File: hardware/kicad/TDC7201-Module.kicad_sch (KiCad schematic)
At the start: 5 parts, among them U2 AMS1117-3.3, U3 TDC7201, U4 TLV3501, U5 TLV3501, U7 ESP32-C3-WROOM-02U-N4

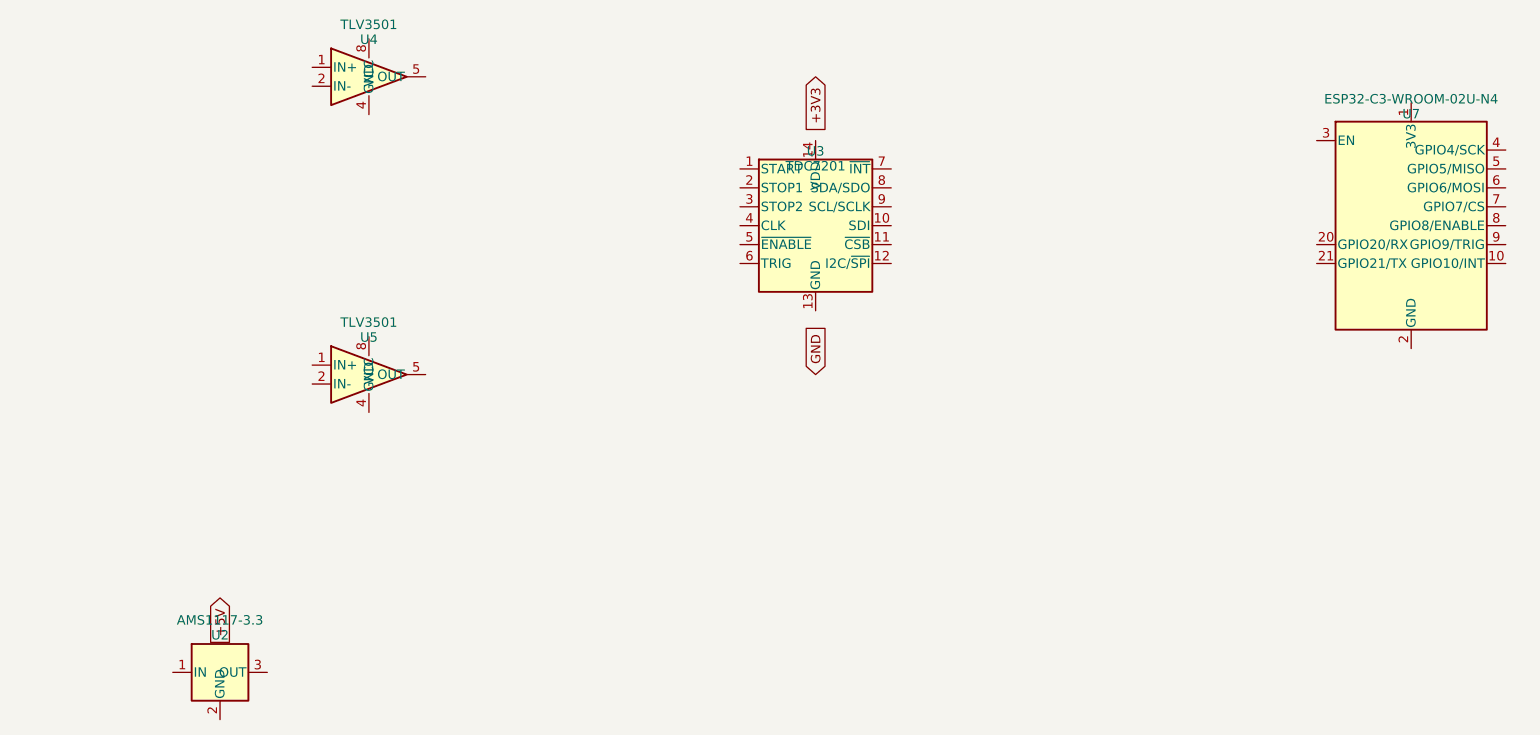
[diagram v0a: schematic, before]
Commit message: Regenerate valid KiCad 7.0 PCB and schematic files
- TDC7201-Module.kicad_pcb: complete rewrite with valid KiCad 7.0
  S-expression syntax (version 20221018). Removes all ;; comments,
  invalid (module ...) / (capacitor ...) / (inductor ...) syntax.
  Adds proper (net 0..15) declarations with numeric IDs, valid
  (footprint ...) blocks for all ICs/connectors with numeric net
  references in pads and vias, 4-layer stackup (F.Cu/In1.Cu/In2.Cu/B.Cu),
  80x50mm board outline on Edge.Cuts, and GND via stitching.
- TDC7201-Module.kicad_sch: complete rewrite removing all ;; comments
  and fixing (net_label ...) to valid (label ...) syntax. Adds
  complete lib_symbols section, properly closed symbol instances,
  global_label declarations, and wire connections.

Agent-Logs-Url: https://github.com/jeffkarney/TDC7201-GPSDO-Module/sessions/249e8e96-76a3-4c3b-a7cb-0897e226d90f

Co-authored-by: jeffkarney <201882+jeffkarney@users.noreply.github.com>
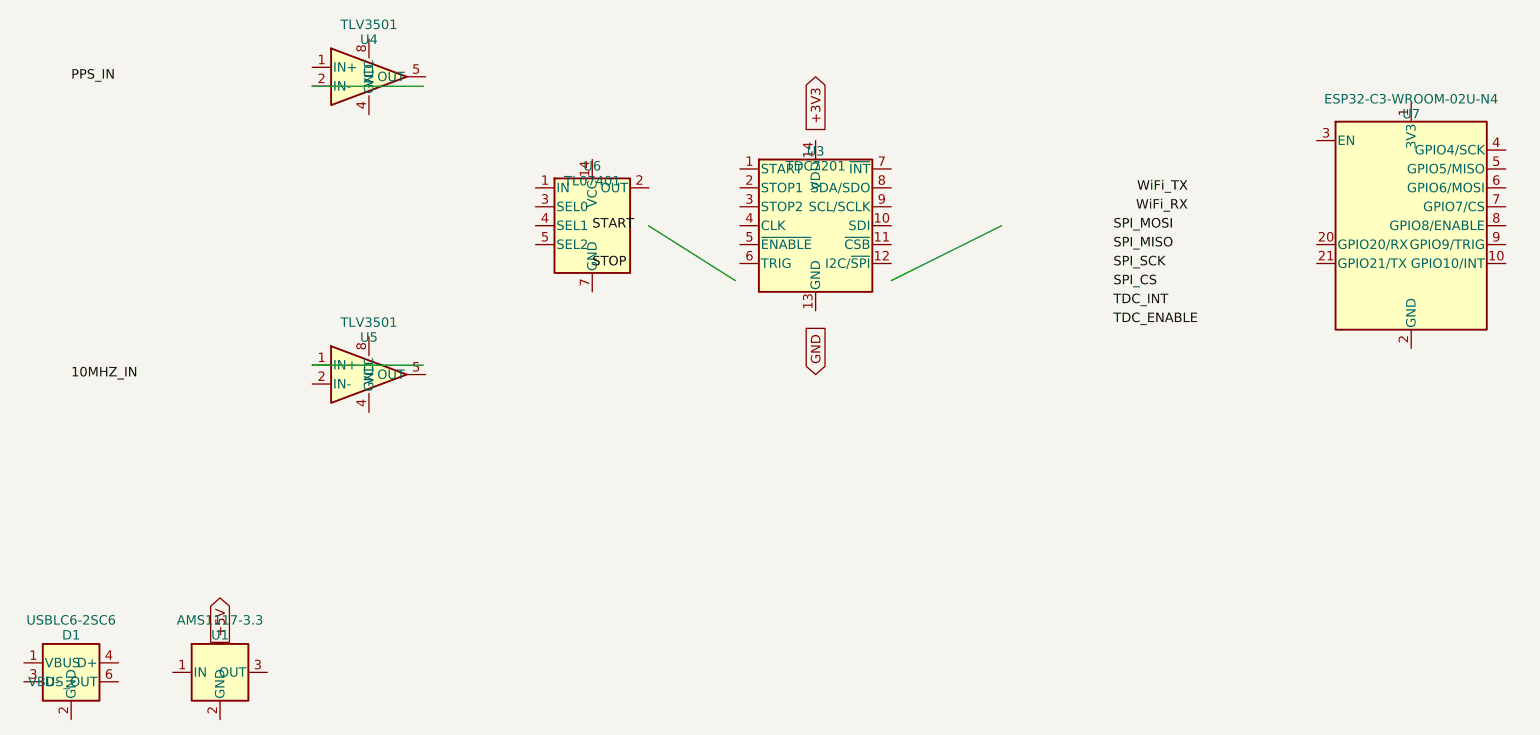
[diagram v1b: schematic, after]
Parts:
- removed U2: AMS1117-3.3, symbol AMS1117-3.3
- added D1: USBLC6-2SC6, Package_TO_SOT_SMD:SOT-23-6, symbol USBLC6-2SC6
- added U1: AMS1117-3.3, Package_TO_SOT_SMD:SOT-223-3_TabPin2, symbol AMS1117-3.3
- added U6: TL07401, Package_SO:TSSOP-14_4.4x5mm_P0.65mm, symbol TL07401
- U4, U5: footprint (none) -> Package_SO:TSSOP-8_3x3mm_P0.65mm
- U7: footprint (none) -> RF_Module:ESP32-C3-WROOM-02
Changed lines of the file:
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@@
 (kicad_sch
-  (version 20231120)
+  (version 20221018)
   (generator "eeschema")
-  (generator_version "7.0")
   (paper "A3")
   (title_block
@@
     (rev "1.0")
     (company "jeffkarney")
-    (comment 1 "4-Layer PCB – JLCPCB JLC04161H-7628")
+    (comment 1 "4-Layer PCB - JLCPCB JLC04161H-7628")
     (comment 2 "ESP32-C3-WROOM-02U-N4 + dual TLV3501 + TDC7201")
     (comment 3 "USB-C 5V input, 3.3V LDO, SPI interface")
   )
-  ;; -------------------------------------------------------------------------
-  ;; Schematic instances (placement)
-  ;; -------------------------------------------------------------------------
-  ;; U3 – TDC7201
   (symbol (lib_id "TDC7201") (at 120 80 0) (unit 1)
     (in_bom yes) (on_board yes)
     (uuid "tdc7201-main-u3")
-    (property "Reference" "U3" (at 120 70 0))
-    (property "Value" "TDC7201" (at 120 72 0))
-    (property "Footprint" "Package_SO:TSSOP-16_4.4x5mm_P0.65mm" (at 0 0 0) (effects (hide yes)))
+    (property "Reference" "U3" (at 120 70 0)
+      (effects (font (size 1.27 1.27))))
+    (property "Value" "TDC7201" (at 120 72 0)
+      (effects (font (size 1.27 1.27))))
+    (property "Footprint" "Package_SO:TSSOP-16_4.4x5mm_P0.65mm" (at 0 0 0)
+      (effects (font (size 1.27 1.27)) (hide yes)))
+    (property "Datasheet" "" (at 0 0 0)
+      (effects (font (size 1.27 1.27)) (hide yes)))
   )
-  ;; U4 – TLV3501 (PPS channel)
   (symbol (lib_id "TLV3501") (at 60 60 0) (unit 1)
     (in_bom yes) (on_board yes)
     (uuid "tlv3501-pps-u4")
-    (property "Reference" "U4" (at 60 55 0))
-    (property "Value" "TLV3501" (at 60 53 0))
+    (property "Reference" "U4" (at 60 55 0)
+      (effects (font (size 1.27 1.27))))
+    (property "Value" "TLV3501" (at 60 53 0)
+      (effects (font (size 1.27 1.27))))
+    (property "Footprint" "Package_SO:TSSOP-8_3x3mm_P0.65mm" (at 0 0 0)
+      (effects (font (size 1.27 1.27)) (hide yes)))
+    (property "Datasheet" "" (at 0 0 0)
+      (effects (font (size 1.27 1.27)) (hide yes)))
   )
-  ;; U5 – TLV3501 (10 MHz reference channel)
   (symbol (lib_id "TLV3501") (at 60 100 0) (unit 1)
     (in_bom yes) (on_board yes)
     (uuid "tlv3501-ref-u5")
-    (property "Reference" "U5" (at 60 95 0))
-    (property "Value" "TLV3501" (at 60 93 0))
+    (property "Reference" "U5" (at 60 95 0)
+      (effects (font (size 1.27 1.27))))
+    (property "Value" "TLV3501" (at 60 93 0)
+      (effects (font (size 1.27 1.27))))
+    (property "Footprint" "Package_SO:TSSOP-8_3x3mm_P0.65mm" (at 0 0 0)
+      (effects (font (size 1.27 1.27)) (hide yes)))
+    (property "Datasheet" "" (at 0 0 0)
+      (effects (font (size 1.27 1.27)) (hide yes)))
   )
-  ;; U7 – ESP32-C3-WROOM-02U-N4
+  (symbol (lib_id "TL07401") (at 90 80 0) (unit 1)
+    (in_bom yes) (on_board yes)
+    (uuid "tl07401-u6")
+    (property "Reference" "U6" (at 90 72 0)
+      (effects (font (size 1.27 1.27))))
+    (property "Value" "TL07401" (at 90 74 0)
+      (effects (font (size 1.27 1.27))))
+    (property "Footprint" "Package_SO:TSSOP-14_4.4x5mm_P0.65mm" (at 0 0 0)
+      (effects (font (size 1.27 1.27)) (hide yes)))
+    (property "Datasheet" "" (at 0 0 0)
+      (effects (font (size 1.27 1.27)) (hide yes)))
+  )
   (symbol (lib_id "ESP32-C3-WROOM-02U") (at 200 80 0) (unit 1)
     (in_bom yes) (on_board yes)
     (uuid "esp32c3-u7")
-    (property "Reference" "U7" (at 200 65 0))
-    (property "Value" "ESP32-C3-WROOM-02U-N4" (at 200 63 0))
+    (property "Reference" "U7" (at 200 65 0)
+      (effects (font (size 1.27 1.27))))
+    (property "Value" "ESP32-C3-WROOM-02U-N4" (at 200 63 0)
+      (effects (font (size 1.27 1.27))))
+    (property "Footprint" "RF_Module:ESP32-C3-WROOM-02" (at 0 0 0)
+      (effects (font (size 1.27 1.27)) (hide yes)))
+    (property "Datasheet" "" (at 0 0 0)
+      (effects (font (size 1.27 1.27)) (hide yes)))
   )
-  ;; U2 – AMS1117-3.3
   (symbol (lib_id "AMS1117-3.3") (at 40 140 0) (unit 1)
     (in_bom yes) (on_board yes)
-    (uuid "ams1117-u2")
-    (property "Reference" "U2" (at 40 135 0))
-    (property "Value" "AMS1117-3.3" (at 40 133 0))
+    (uuid "ams1117-u1")
+    (property "Reference" "U1" (at 40 135 0)
+      (effects (font (size 1.27 1.27))))
+    (property "Value" "AMS1117-3.3" (at 40 133 0)
+      (effects (font (size 1.27 1.27))))
+    (property "Footprint" "Package_TO_SOT_SMD:SOT-223-3_TabPin2" (at 0 0 0)
+      (effects (font (size 1.27 1.27)) (hide yes)))
+    (property "Datasheet" "" (at 0 0 0)
+      (effects (font (size 1.27 1.27)) (hide yes)))
   )
-  ;; -------------------------------------------------------------------------
-  ;; Power nets and labels
-  ;; -------------------------------------------------------------------------
+  (symbol (lib_id "USBLC6-2SC6") (at 20 140 0) (unit 1)
+    (in_bom yes) (on_board yes)
+    (uuid "usblc6-d1")
+    (property "Reference" "D1" (at 20 135 0)
+      (effects (font (size 1.27 1.27))))
+    (property "Value" "USBLC6-2SC6" (at 20 133 0)
+      (effects (font (size 1.27 1.27))))
+    (property "Footprint" "Package_TO_SOT_SMD:SOT-23-6" (at 0 0 0)
+      (effects (font (size 1.27 1.27)) (hide yes)))
+    (property "Datasheet" "" (at 0 0 0)
+      (effects (font (size 1.27 1.27)) (hide yes)))
+  )
   (global_label "+3V3" (shape input) (at 120 60 270)
     (effects (font (size 1.27 1.27)))
-    (uuid "pwr-3v3-tdc"))
+    (uuid "pwr-3v3-tdc")
+    (property "Intersheet References" "${INTERSHEET_REFS}" (at 0 0 0)
+      (effects (font (size 1.27 1.27)) (hide yes)))
+  )
   (global_label "+5V" (shape input) (at 40 130 270)
     (effects (font (size 1.27 1.27)))
-    (uuid "pwr-5v-vreg"))
+    (uuid "pwr-5v-vreg")
+    (property "Intersheet References" "${INTERSHEET_REFS}" (at 0 0 0)
+      (effects (font (size 1.27 1.27)) (hide yes)))
+  )
   (global_label "GND" (shape input) (at 120 100 90)
     (effects (font (size 1.27 1.27)))
-    (uuid "pwr-gnd-tdc"))
-  ;; -------------------------------------------------------------------------
-  ;; Net labels for key signals
-  ;; -------------------------------------------------------------------------
-  (net_label "START" (at 90 80 0) (uuid "net-start"))
-  (net_label "STOP" (at 90 85 0) (uuid "net-stop"))
-  (net_label "SPI_MOSI" (at 160 80 0) (uuid "net-mosi"))
-  (net_label "SPI_MISO" (at 160 82 0) (uuid "net-miso"))
-  (net_label "SPI_SCK" (at 160 84 0) (uuid "net-sck"))
-  (net_label "SPI_CS" (at 160 86 0) (uuid "net-cs"))
-  (net_label "TDC_INT" (at 160 88 0) (uuid "net-int"))
-  (net_label "TDC_ENABLE" (at 160 90 0) (uuid "net-enable"))
-  ;; -------------------------------------------------------------------------
-  ;; Schematic-level wires (abbreviated – key connections shown)
-  ;;
-  ;; J1 (SMA PPS) → R_TERM1 → C_AC1 → U4.IN+ → (TL07401 delay) → U3.START
-  ;; J2 (SMA 10MHz) → R_TERM2 → C_AC2 → U5.IN+ → U3.STOP1
-  ;; U3.SDO/SDA → U7.GPIO5 (MISO)
-  ;; U3.SCLK/SCL → U7.GPIO4 (SCK)
-  ;; U3.SDI → U7.GPIO6 (MOSI)
-  ;; U3.~{CSB} → U7.GPIO7 (CS)
-  ;; U3.~{INT} → U7.GPIO10
-  ;; U3.ENABLE → U7.GPIO8
-  ;; U3.TRIG → U7.GPIO9
-  ;; U2.IN ← +5V (USB-C through ESD diode)
-  ;; U2.OUT → +3V3 (TDC7201, ESP32-C3)
-  ;; -------------------------------------------------------------------------
-  ;; -------------------------------------------------------------------------
-  ;; Decoupling capacitors (representative – all 100 nF 0603 X5R)
-  ;; -------------------------------------------------------------------------
-  ;; C1–C10: 100 nF decoupling near each IC power pin
-  ;; C11–C12: 10 µF bulk at USB input and LDO output
-  ;; L1–L2: BLM21PG221SN1D ferrite beads (analog/digital power separation)
-  ;; -------------------------------------------------------------------------
-  ;; Test points (TP1–TP12)
-  ;; TP1: +5V rail       TP2: GND            TP3: +3V3 rail
-  ;; TP4: START signal   TP5: STOP signal     TP6: TDC7201 CLK
-  ;; TP7: SPI_SCK        TP8: SPI_MOSI        TP9: SPI_MISO
-  ;; TP10: TDC_INT       TP11: PPS_IN (raw)   TP12: 10MHz_IN (raw)
-  ;; -------------------------------------------------------------------------
-  ;; -------------------------------------------------------------------------
-  ;; SMA Connectors
-  ;; J1: PPS Input (SMA)
-  ;; J2: 10 MHz Reference Input (SMA)
-  ;; J3: WiFi Antenna (SMA / IPX)
-  ;; -------------------------------------------------------------------------
+    (uuid "pwr-gnd-tdc")
+    (property "Intersheet References" "${INTERSHEET_REFS}" (at 0 0 0)
+      (effects (font (size 1.27 1.27)) (hide yes)))
+  )
+  (label "START" (at 90 80 0)
+    (effects (font (size 1.27 1.27)))
+    (uuid "net-start"))
+  (label "STOP" (at 90 85.08 0)
+    (effects (font (size 1.27 1.27)))
+    (uuid "net-stop"))
+  (label "SPI_MOSI" (at 160 80 0)
+    (effects (font (size 1.27 1.27)))
+    (uuid "net-mosi"))
+  (label "SPI_MISO" (at 160 82.54 0)
+    (effects (font (size 1.27 1.27)))
+    (uuid "net-miso"))
+  (label "SPI_SCK" (at 160 85.08 0)
+    (effects (font (size 1.27 1.27)))
+    (uuid "net-sck"))
+  (label "SPI_CS" (at 160 87.62 0)
+    (effects (font (size 1.27 1.27)))
+    (uuid "net-cs"))
+  (label "TDC_INT" (at 160 90.16 0)
+    (effects (font (size 1.27 1.27)))
+    (uuid "net-int"))
+  (label "TDC_ENABLE" (at 160 92.70 0)
+    (effects (font (size 1.27 1.27)))
+    (uuid "net-enable"))
+  (label "PPS_IN" (at 20 60 0)
+    (effects (font (size 1.27 1.27)))
+    (uuid "net-ppsin"))
+  (label "10MHZ_IN" (at 20 100 0)
+    (effects (font (size 1.27 1.27)))
+    (uuid "net-10mhz"))
+  (label "WiFi_RX" (at 170 77.46 180)
+    (effects (font (size 1.27 1.27)))
+    (uuid "net-wifi-rx"))
+  (label "WiFi_TX" (at 170 74.92 180)
+    (effects (font (size 1.27 1.27)))
+    (uuid "net-wifi-tx"))
+  (wire (pts (xy 52.38 61.27) (xy 67.31 61.27))
+    (uuid "wire-u4out-start"))
+  (wire (pts (xy 52.38 98.73) (xy 67.31 98.73))
+    (uuid "wire-u5out-stop"))
+  (wire (pts (xy 97.54 80) (xy 109.22 87.38))
+    (uuid "wire-u6out-tdc"))
+  (wire (pts (xy 130.16 87.38) (xy 145.0 80))
+    (uuid "wire-tdc-spi"))
 )
